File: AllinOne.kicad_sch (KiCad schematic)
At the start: 15 parts, among them P1 USB_C_Plug_USB2.0, SW1 SW_Push, U1 AT90USB1286-AU, Y1 16MHz

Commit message: Schematic all done
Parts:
- removed P1: USB_C_Plug_USB2.0, symbol Connector:USB_C_Plug_USB2.0
- added D1, D2, D3, D4: SOD-123, Diode_SMD:D_SOD-123, symbol Device:D_Small
- added F1: 500mA, Fuse:Fuse_1206_3216Metric, symbol Device:Polyfuse_Small
- added J1: USB_B_Mini, Connector_USB:USB3_A_Molex_48393-001, symbol Connector:USB_B_Mini
- added SW0, SW1, SW2, SW3: SW_Push, Button_Switch_Keyboard:SW_Cherry_MX_1.00u_PCB, symbol Switch:SW_Push
- C1, C2, C3, C4, C5, C6, C7: footprint (none) -> Capacitor_SMD:C_0805_2012Metric
- R1, R4: value 1k -> 10k; footprint (none) -> Resistor_SMD:R_0805_2012Metric
- R2, R3: footprint (none) -> Resistor_SMD:R_0805_2012Metric
- SW_R1: renamed from SW1; footprint (none) -> Button_Switch_THT:SW_PUSH_6mm
- U1: footprint (none) -> CustomMCUs:AT90USB1286-AU
- Y1: footprint (none) -> Crystal:Crystal_SMD_3225-4Pin_3.2x2.5mm
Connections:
- net +5V: now also F1.1
- net GND: now also J1.5 (GND)
- net D-: now reaches R3.2
- net D-: now also J1.2 (D-)
- net at R1.1: now also U1.43 (PE2); no longer U1.34 (PE1)
- net D+: now reaches R2.2
- net D+: now also J1.3 (D+)
- new net: D1.2 (A), SW0.1
- new net: D2.2 (A), SW1.1
- new net: D3.2 (A), SW2.1
- new net: D4.2 (A), SW3.1
- new net COL_0: SW0.2, SW2.2
- new net COL_1: SW1.2, SW3.2
- new net ROW_0: D1.1 (K), D2.1 (K)
- new net ROW_1: D3.1 (K), D4.1 (K)
- new net VCC: F1.2, J1.1 (VBUS)
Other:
- moved on the sheet: C1, C2, C3, C4, C5, C6, C7, R1, R2, R3, R4, SW_R1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

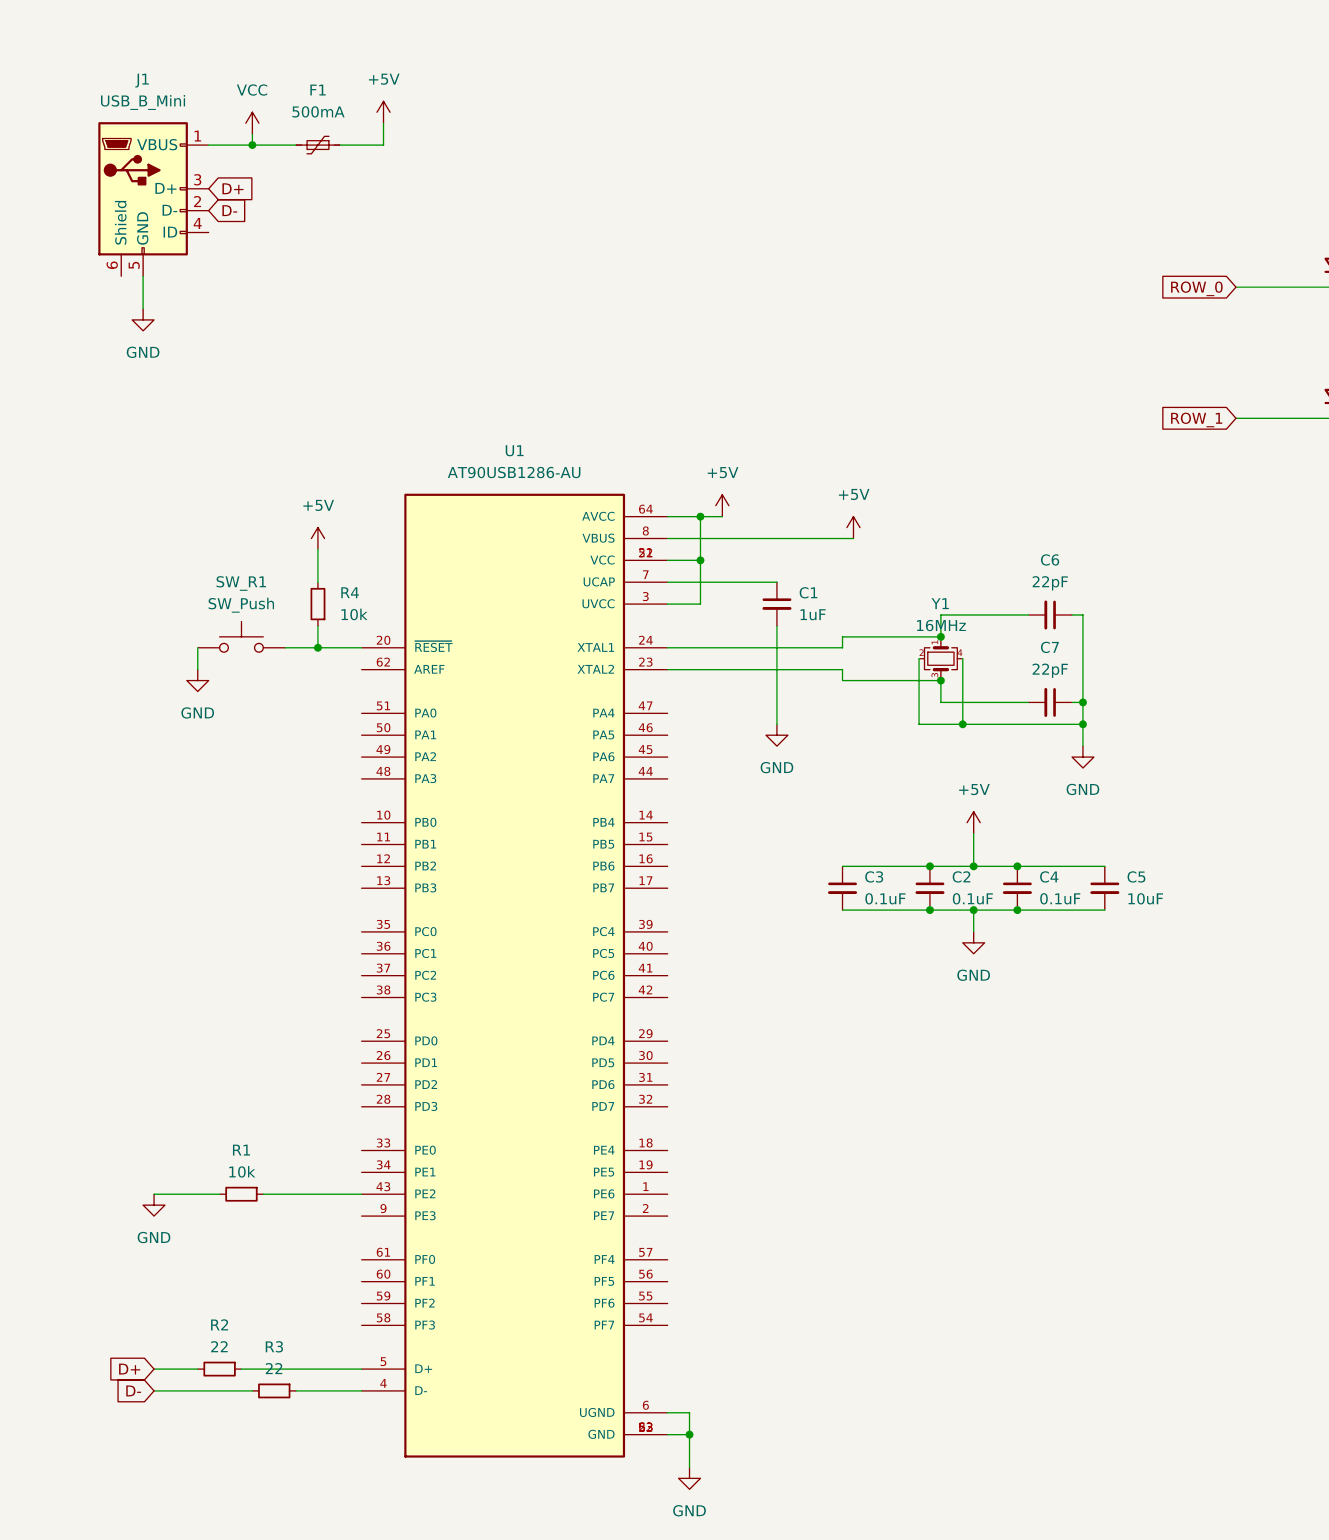
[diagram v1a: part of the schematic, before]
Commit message: Wired MCU
Wired the 32U4 and updated the schematic just needs to add all switches
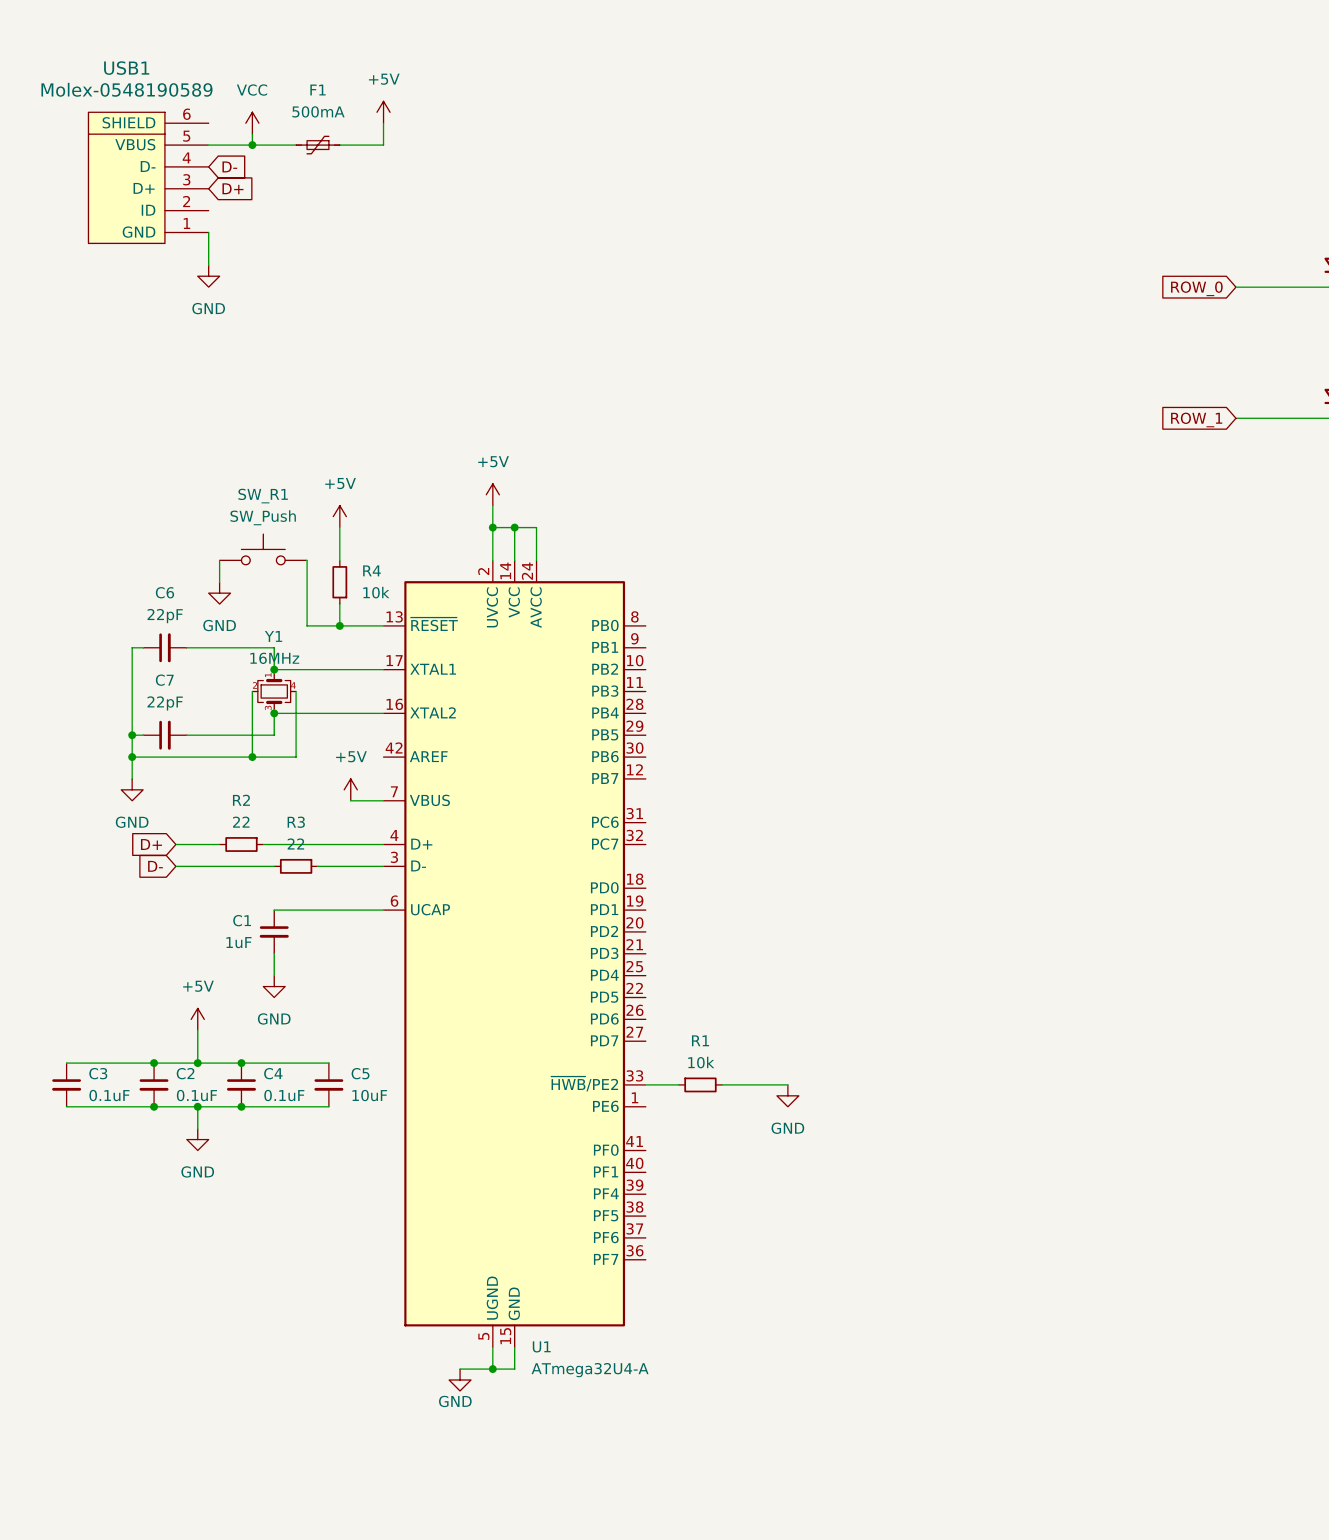
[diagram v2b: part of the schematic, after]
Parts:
- removed J1: USB_B_Mini, Connector_USB:USB3_A_Molex_48393-001, symbol Connector:USB_B_Mini
- removed U1: AT90USB1286-AU, CustomMCUs:AT90USB1286-AU, symbol CustomMCU:AT90USB1286-AU
- added U1: ATmega32U4-A, Package_QFP:TQFP-44_10x10mm_P0.8mm, symbol MCU_Microchip_ATmega:ATmega32U4-A
- added USB1: Molex-0548190589, random-keyboard-parts.pretty-master:Molex-0548190589, symbol random-keyboard-parts:Molex-0548190589
- SW_R1: footprint Button_Switch_THT:SW_PUSH_6mm -> random-keyboard-parts.pretty-master:SKQG-1155865
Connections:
- net +5V: now also U1.14 (VCC), U1.2 (UVCC), U1.24 (AVCC), U1.34 (VCC), U1.44 (AVCC), U1.7 (VBUS)
- net D+: now also USB1.3 (D+)
- net D-: now also USB1.4 (D-)
- net GND: now also U1.15 (GND), U1.23 (GND), U1.35 (GND), U1.43 (GND), U1.5 (UGND), USB1.1 (GND)
- net VCC: now also USB1.5 (VBUS)
- net at C1.1: now also U1.6 (UCAP)
- net at R3.1: now also U1.3 (D-)
- net at R1.1: now also U1.33 (~{HWB}/PE2)
- net at C6.2, Y1.1: now also U1.17 (XTAL1)
- net at R4.1, SW_R1.2: now also U1.13 (~{RESET})
- net at R2.1: now also U1.4 (D+)
- net at C7.2, Y1.3: now also U1.16 (XTAL2)
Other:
- moved on the sheet: C1, C2, C3, C4, C5, C6, C7, R1, R2, R3, R4, SW_R1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

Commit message: Started organizing switches
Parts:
- removed D2, D3, D4: SOD-123, Diode_SMD:D_SOD-123, symbol Device:D_Small
- added D10, D100, D101, D102, D103, D104, D105, D106, D107, D108, D109, D11, D110, D111, D112, D113, D114, D115, D116, D119, D12, D121, D122, D123, D124, D125, D126, D127, D13, D131, D135, D136, D137, D138, D139, D14, D140, D141, D142, D143, D144, D15, D16, D17, D18, D19, D20, D23, D24, D25, D26, D27, D28, D29, D30, D31, D32, D33, D34, D35, D36, D37, D38, D39, D40, D41, D42, D43, D44, D45, D46, D47, D48, D49, D5, D50, D51, D52, D53, D54, D55, D56, D57, D58, D6, D60, D61, D62, D63, D64, D65, D66, D67, D68, D69, D7, D70, D71, D72, D73, D74, D75, D76, D77, D79, D8, D80, D81, D82, D83, D84, D85, D86, D87, D88, D89, D9, D90, D91, D92, D93, D94, D95, D96, D97: SOD-123, Diode_SMD:D_SOD-123, symbol Device:D_Small
- added SW10, SW100, SW101, SW102, SW103, SW104, SW105, SW106, SW107, SW108, SW109, SW11, SW110, SW111, SW114, SW116, SW117, SW118, SW119, SW12, SW120, SW121, SW122, SW13, SW130, SW131, SW132, SW133, SW134, SW135, SW136, SW137, SW138, SW139, SW14, SW15, SW18, SW19, SW20, SW21, SW22, SW23, SW24, SW25, SW26, SW27, SW28, SW29, SW30, SW31, SW32, SW33, SW34, SW35, SW36, SW37, SW38, SW39, SW4, SW40, SW41, SW42, SW43, SW44, SW45, SW46, SW47, SW48, SW49, SW5, SW50, SW51, SW52, SW55, SW56, SW57, SW58, SW59, SW6, SW60, SW61, SW62, SW63, SW64, SW65, SW66, SW67, SW68, SW69, SW7, SW70, SW71, SW72, SW75, SW76, SW77, SW78, SW79, SW8, SW80, SW81, SW82, SW83, SW84, SW85, SW86, SW87, SW88, SW89, SW9, SW90, SW91, SW92, SW95, SW96, SW97, SW98, SW99: SW_Push, Button_Switch_Keyboard:SW_Cherry_MX_1.00u_PCB, symbol Switch:SW_Push
- added SW126: SW_Push, Button_Switch_Keyboard:SW_Cherry_MX_6.25u_PCB, symbol Switch:SW_Push
- added SW16, SW53, SW74: SW_Push, Button_Switch_Keyboard:SW_Cherry_MX_2.00u_PCB, symbol Switch:SW_Push
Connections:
- net COL_0: now also SW1.2, SW100.2, SW101.2, SW120.2, SW121.2, SW20.2, SW21.2, SW40.2, SW41.2, SW60.2, SW61.2, SW80.2, SW81.2; no longer SW2.2
- net COL_1: now also SW2.2, SW102.2, SW103.2, SW122.2, SW22.2, SW23.2, SW42.2, SW43.2, SW62.2, SW63.2, SW82.2, SW83.2; no longer SW1.2
- net ROW_0: now also D11.1 (K), D13.1 (K), D15.1 (K), D17.1 (K), D19.1 (K), D23.1 (K), D5.1 (K), D7.1 (K), D9.1 (K); no longer D1.1 (K)
- net ROW_1: now also D10.1 (K), D12.1 (K), D14.1 (K), D16.1 (K), D18.1 (K), D20.1 (K), D24.1 (K), D6.1 (K), D8.1 (K)
- net at SW0.1: now also D5.2 (A); no longer D1.2 (A)
- net at SW1.1: now also D6.2 (A)
- net at SW2.1: now also D7.2 (A)
- net at SW3.1: now also D8.2 (A)
- new net: D12.2 (A), SW7.1
- new net: D62.2 (A), SW57.1
- new net: D74.2 (A), SW69.1
- new net: D123.2 (A), SW118.1
- new net: D141.2 (A), SW136.1
- new net: D60.2 (A), SW55.1
- new net: D20.2 (A), SW15.1
- new net: D36.2 (A), SW31.1
- new net: D52.2 (A), SW47.1
- new net: D84.2 (A), SW79.1
- new net: D10.2 (A), SW5.1
- new net: D42.2 (A), SW37.1
- new net: D38.2 (A), SW33.1
- new net: D56.2 (A), SW51.1
- new net: D65.2 (A), SW60.1
- new net: D135.2 (A), SW130.1
- new net: D111.2 (A), SW106.1
- new net: D28.2 (A), SW23.1
- new net: D13.2 (A), SW8.1
- new net: D14.2 (A), SW9.1
- new net: D138.2 (A), SW133.1
- new net: D93.2 (A), SW88.1
- new net: D66.2 (A), SW61.1
- new net: D31.2 (A), SW26.1
- new net: D71.2 (A), SW66.1
- new net: D50.2 (A), SW45.1
- new net: D86.2 (A), SW81.1
- new net: D105.2 (A), SW100.1
- new net: D97.2 (A), SW92.1
- new net: D109.2 (A), SW104.1
- new net: D15.2 (A), SW10.1
- new net: D87.2 (A), SW82.1
- new net: D94.2 (A), SW89.1
- new net: D88.2 (A), SW83.1
- new net: D67.2 (A), SW62.1
- new net: D89.2 (A), SW84.1
- new net: D61.2 (A), SW56.1
- new net: D91.2 (A), SW86.1
- new net: D77.2 (A), SW72.1
- new net: D19.2 (A), SW14.1
- new net: D26.2 (A), SW21.1
- new net: D107.2 (A), SW102.1
- new net: D119.2 (A), SW114.1
- new net: D40.2 (A), SW35.1
- new net: D24.2 (A), SW19.1
- new net: D27.2 (A), SW22.1
- new net: D90.2 (A), SW85.1
- new net: D57.2 (A), SW52.1
- new net: D101.2 (A), SW96.1
- new net: D83.2 (A), SW78.1
- new net: D110.2 (A), SW105.1
- new net: D9.2 (A), SW4.1
- new net: D106.2 (A), SW101.1
- new net: D116.2 (A), SW111.1
- new net: D45.2 (A), SW40.1
- new net: D95.2 (A), SW90.1
- new net: D140.2 (A), SW135.1
- new net: D64.2 (A), SW59.1
- new net: D125.2 (A), SW120.1
- new net: D49.2 (A), SW44.1
- new net: D70.2 (A), SW65.1
- new net: D143.2 (A), SW138.1
- new net: D81.2 (A), SW76.1
- new net: D144.2 (A), SW139.1
- new net: D121.2 (A), SW116.1
- new net: D122.2 (A), SW117.1
- new net: D102.2 (A), SW97.1
- new net: D108.2 (A), SW103.1
- new net: D85.2 (A), SW80.1
- new net: D112.2 (A), SW107.1
- new net: D82.2 (A), SW77.1
- new net: D46.2 (A), SW41.1
- new net: D55.2 (A), SW50.1
- new net: D32.2 (A), SW27.1
- new net: D104.2 (A), SW99.1
- new net: D76.2 (A), SW71.1
- new net: D92.2 (A), SW87.1
- new net: D96.2 (A), SW91.1
- new net: D23.2 (A), SW18.1
- new net: D63.2 (A), SW58.1
- new net: D100.2 (A), SW95.1
- new net: D35.2 (A), SW30.1
- new net: D16.2 (A), SW11.1
- new net: D54.2 (A), SW49.1
- new net: D53.2 (A), SW48.1
- new net: D41.2 (A), SW36.1
- new net: D44.2 (A), SW39.1
- new net: D69.2 (A), SW64.1
- new net: D131.2 (A), SW126.1
- new net: D124.2 (A), SW119.1
- new net: D114.2 (A), SW109.1
- new net: D51.2 (A), SW46.1
- new net: D29.2 (A), SW24.1
- new net: D18.2 (A), SW13.1
- new net: D68.2 (A), SW63.1
- new net: D43.2 (A), SW38.1
- new net: D115.2 (A), SW110.1
- new net: D127.2 (A), SW122.1
- new net: D33.2 (A), SW28.1
- new net: D58.2 (A), SW53.1
- new net: D25.2 (A), SW20.1
- new net: D80.2 (A), SW75.1
- new net: D136.2 (A), SW131.1
- new net: D47.2 (A), SW42.1
- new net: D113.2 (A), SW108.1
- new net: D34.2 (A), SW29.1
- new net: D30.2 (A), SW25.1
- new net: D73.2 (A), SW68.1
- new net: D1.2 (A), SW16.1
- new net: D75.2 (A), SW70.1
- new net: D137.2 (A), SW132.1
- new net: D142.2 (A), SW137.1
- new net: D79.2 (A), SW74.1
- new net: D48.2 (A), SW43.1
- new net: D103.2 (A), SW98.1
- new net: D72.2 (A), SW67.1
- new net: D37.2 (A), SW32.1
- new net: D126.2 (A), SW121.1
- new net: D39.2 (A), SW34.1
- new net: D139.2 (A), SW134.1
- new net: D11.2 (A), SW6.1
- new net: D17.2 (A), SW12.1
- new net COL_2: SW104.2, SW105.2, SW24.2, SW25.2, SW4.2, SW44.2, SW45.2, SW5.2, SW64.2, SW65.2, SW84.2, SW85.2
- new net COL_3: SW106.2, SW107.2, SW126.2, SW26.2, SW27.2, SW46.2, SW47.2, SW6.2, SW66.2, SW67.2, SW7.2, SW86.2, SW87.2
- new net COL_4: SW108.2, SW109.2, SW28.2, SW29.2, SW48.2, SW49.2, SW68.2, SW69.2, SW8.2, SW88.2, SW89.2, SW9.2
- new net COL_5: SW10.2, SW11.2, SW110.2, SW130.2, SW131.2, SW30.2, SW31.2, SW50.2, SW51.2, SW70.2, SW71.2, SW90.2, SW91.2
- new net COL_6: SW111.2, SW12.2, SW13.2, SW132.2, SW133.2, SW32.2, SW33.2, SW52.2, SW72.2, SW92.2
- new net COL_7: SW114.2, SW134.2, SW135.2, SW14.2, SW15.2, SW16.2, SW34.2, SW35.2, SW53.2, SW55.2, SW74.2, SW75.2, SW95.2
- new net COL_8: SW116.2, SW117.2, SW136.2, SW137.2, SW36.2, SW37.2, SW56.2, SW57.2, SW76.2, SW77.2, SW96.2, SW97.2
- new net COL_9: SW118.2, SW119.2, SW138.2, SW139.2, SW18.2, SW19.2, SW38.2, SW39.2, SW58.2, SW59.2, SW78.2, SW79.2, SW98.2, SW99.2
- new net ROW_10: D105.1 (K), D107.1 (K), D109.1 (K), D111.1 (K), D113.1 (K), D115.1 (K), D116.1 (K), D119.1 (K), D121.1 (K), D123.1 (K)
- new net ROW_11: D106.1 (K), D108.1 (K), D110.1 (K), D112.1 (K), D114.1 (K), D122.1 (K), D124.1 (K)
- new net ROW_12: D125.1 (K), D127.1 (K), D131.1 (K), D135.1 (K), D137.1 (K), D139.1 (K), D141.1 (K), D143.1 (K)
- new net ROW_13: D126.1 (K), D136.1 (K), D138.1 (K), D140.1 (K), D142.1 (K), D144.1 (K)
- new net ROW_2: D25.1 (K), D27.1 (K), D29.1 (K), D31.1 (K), D33.1 (K), D35.1 (K), D37.1 (K), D39.1 (K), D41.1 (K), D43.1 (K)
- new net ROW_3: D26.1 (K), D28.1 (K), D30.1 (K), D32.1 (K), D34.1 (K), D36.1 (K), D38.1 (K), D40.1 (K), D42.1 (K), D44.1 (K)
- new net ROW_4: D45.1 (K), D47.1 (K), D49.1 (K), D51.1 (K), D53.1 (K), D55.1 (K), D57.1 (K), D58.1 (K), D61.1 (K), D63.1 (K)
- new net ROW_5: D46.1 (K), D48.1 (K), D50.1 (K), D52.1 (K), D54.1 (K), D56.1 (K), D60.1 (K), D62.1 (K), D64.1 (K)
- new net ROW_6: D1.1 (K), D65.1 (K), D67.1 (K), D69.1 (K), D71.1 (K), D73.1 (K), D75.1 (K), D77.1 (K), D81.1 (K), D83.1 (K)
- new net ROW_7: D66.1 (K), D68.1 (K), D70.1 (K), D72.1 (K), D74.1 (K), D76.1 (K), D80.1 (K), D82.1 (K), D84.1 (K)
- new net ROW_8: D101.1 (K), D103.1 (K), D79.1 (K), D85.1 (K), D87.1 (K), D89.1 (K), D91.1 (K), D93.1 (K), D95.1 (K), D97.1 (K)
- new net ROW_9: D100.1 (K), D102.1 (K), D104.1 (K), D86.1 (K), D88.1 (K), D90.1 (K), D92.1 (K), D94.1 (K), D96.1 (K)
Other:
- title: (none) -> ALLINKB
- moved on the sheet: C1, C2, C3, C4, C5, C6, C7, F1, R1, R2, R3, R4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

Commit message: Finished switch lineup
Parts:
- SW111: footprint Button_Switch_Keyboard:SW_Cherry_MX_1.00u_PCB -> Button_Switch_Keyboard:SW_Cherry_MX_2.00u_PCB
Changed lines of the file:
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@@
       (effects (font (size 1.27 1.27)))
     )
-    (property "Footprint" "Button_Switch_Keyboard:SW_Cherry_MX_1.00u_PCB" (at 256.54 127 0)
+    (property "Footprint" "Button_Switch_Keyboard:SW_Cherry_MX_2.00u_PCB" (at 256.54 127 0)
       (effects (font (size 1.27 1.27)) hide)
     )

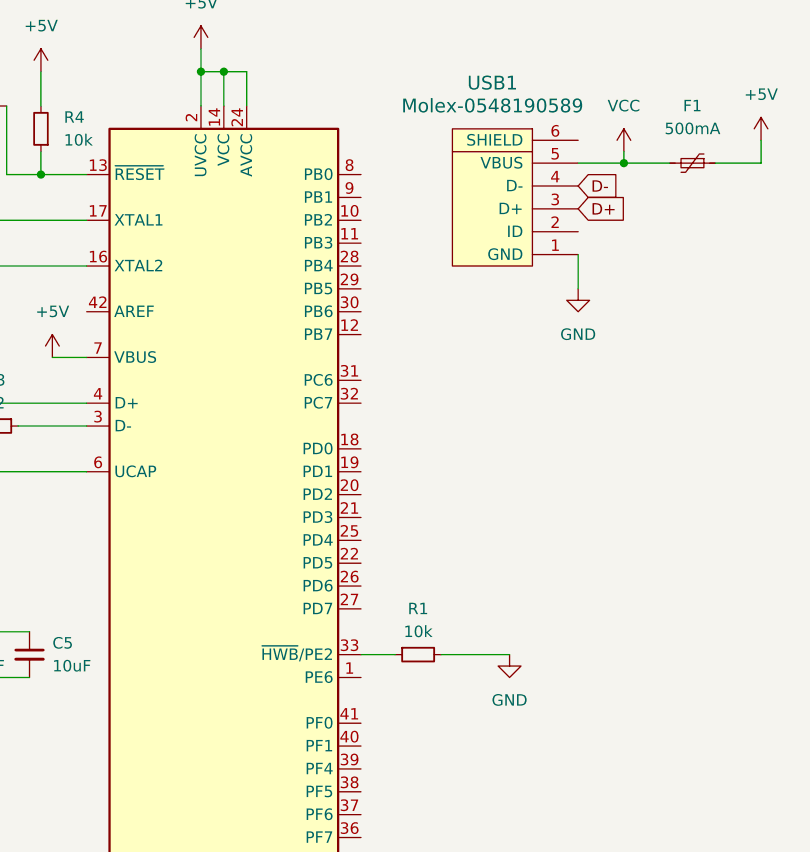
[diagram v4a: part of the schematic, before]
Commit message: Started routing to MCU
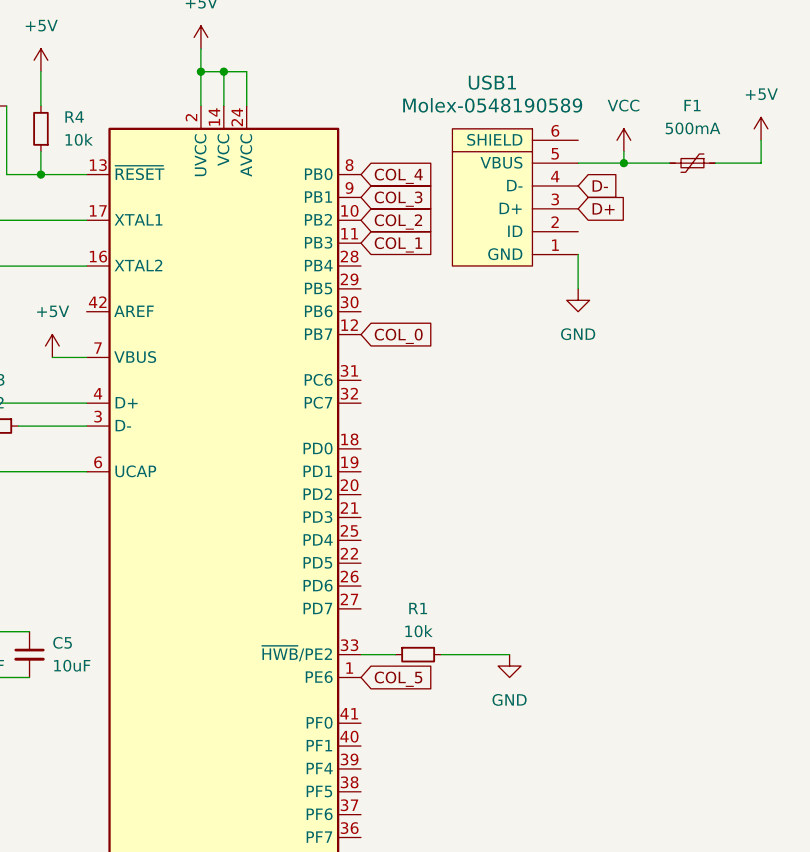
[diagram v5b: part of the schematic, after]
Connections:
- net COL_0: now also U1.12 (PB7)
- net COL_1: now also U1.11 (PB3)
- net COL_2: now also U1.10 (PB2)
- net COL_3: now also U1.9 (PB1)
- net COL_4: now also U1.8 (PB0)
- net COL_5: now also U1.1 (PE6)
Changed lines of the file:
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@@
+    )
+  )
+  (global_label "COL_1" (shape input) (at 87.63 186.69 0) (fields_autoplaced)
+    (effects (font (size 1.27 1.27)) (justify left))
+    (property "Intersheetrefs" "${INTERSHEET_REFS}" (at 96.3415 186.69 0)
+      (effects (font (size 1.27 1.27)) (justify left) hide)
     )
   )
@@
     )
   )
+  (global_label "COL_3" (shape input) (at 87.63 181.61 0) (fields_autoplaced)
+    (effects (font (size 1.27 1.27)) (justify left))
+    (property "Intersheetrefs" "${INTERSHEET_REFS}" (at 96.3415 181.61 0)
+      (effects (font (size 1.27 1.27)) (justify left) hide)
+    )
+  )
+  (global_label "COL_4" (shape input) (at 87.63 179.07 0) (fields_autoplaced)
+    (effects (font (size 1.27 1.27)) (justify left))
+    (property "Intersheetrefs" "${INTERSHEET_REFS}" (at 96.3415 179.07 0)
+      (effects (font (size 1.27 1.27)) (justify left) hide)
+    )
+  )
   (global_label "D+" (shape input) (at 33.02 204.47 180) (fields_autoplaced)
     (effects (font (size 1.27 1.27)) (justify right))
@@
     (effects (font (size 1.27 1.27)) (justify left))
     (property "Intersheetrefs" "${INTERSHEET_REFS}" (at 218.44 19.2285 90)
+      (effects (font (size 1.27 1.27)) (justify left) hide)
+    )
+  )
+  (global_label "COL_5" (shape input) (at 87.63 234.95 0) (fields_autoplaced)
+    (effects (font (size 1.27 1.27)) (justify left))
+    (property "Intersheetrefs" "${INTERSHEET_REFS}" (at 96.3415 234.95 0)
       (effects (font (size 1.27 1.27)) (justify left) hide)
     )
@@
     )
   )
+  (global_label "COL_0" (shape input) (at 87.63 196.85 0) (fields_autoplaced)
+    (effects (font (size 1.27 1.27)) (justify left))
+    (property "Intersheetrefs" "${INTERSHEET_REFS}" (at 96.3415 196.85 0)
+      (effects (font (size 1.27 1.27)) (justify left) hide)
+    )
+  )
   (global_label "D-" (shape input) (at 111.76 180.34 0) (fields_autoplaced)
     (effects (font (size 1.27 1.27)) (justify left))
@@
     )
   )
+  (global_label "COL_2" (shape input) (at 87.63 184.15 0) (fields_autoplaced)
+    (effects (font (size 1.27 1.27)) (justify left))
+    (property "Intersheetrefs" "${INTERSHEET_REFS}" (at 96.3415 184.15 0)
+      (effects (font (size 1.27 1.27)) (justify left) hide)
+    )
+  )
